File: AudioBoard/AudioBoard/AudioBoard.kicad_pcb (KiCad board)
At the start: 2 copper layers, 14 parts, among them U5 TL072

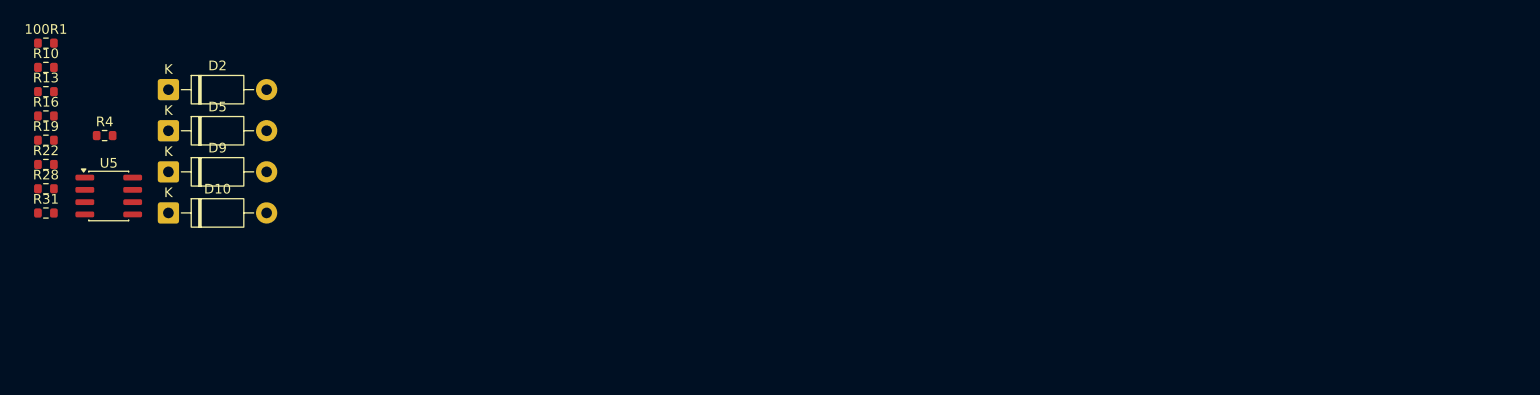
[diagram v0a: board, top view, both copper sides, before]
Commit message: input section with templates are working
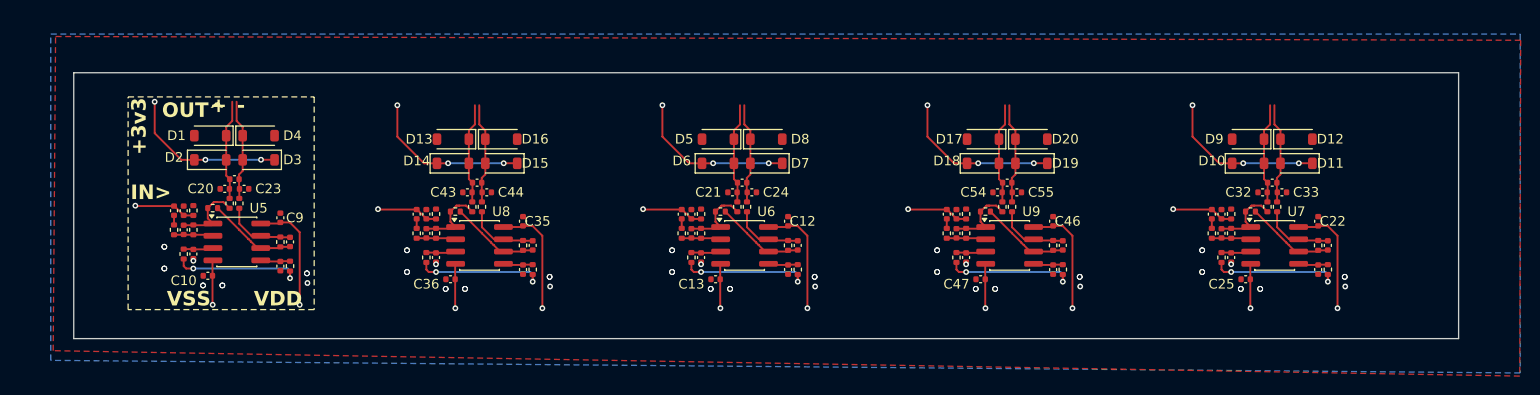
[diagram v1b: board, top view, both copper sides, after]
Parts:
- added 100R2: 1k, Resistor_SMD:R_0402_1005Metric, F.Cu at (112.5, 63.1)
- added 100R3: 1k, Resistor_SMD:R_0402_1005Metric, F.Cu at (167.3, 63.1)
- added 100R4: 1k, Resistor_SMD:R_0402_1005Metric, F.Cu at (85.1, 63.1)
- added 100R5: 1k, Resistor_SMD:R_0402_1005Metric, F.Cu at (139.9, 63.1)
- added C10: 100n, Capacitor_SMD:C_0402_1005Metric, F.Cu at (51.5, 63.8)
- added C11: 1p, Capacitor_SMD:C_0402_1005Metric, F.Cu at (49.0, 59.0)
- added C12: 100n, Capacitor_SMD:C_0402_1005Metric, F.Cu at (111.5, 58.1)
- added C13: 100n, Capacitor_SMD:C_0402_1005Metric, F.Cu at (104.0, 64.1)
- added C14: 100p, Capacitor_SMD:C_0402_1005Metric, F.Cu at (60.0, 60.2)
- added C15: 100n, Capacitor_SMD:C_0402_1005Metric, F.Cu at (102.5, 61.9)
- added C16: 1p, Capacitor_SMD:C_0402_1005Metric, F.Cu at (101.5, 59.4)
- added C17: 100n, Capacitor_SMD:C_0402_1005Metric, F.Cu at (59.0, 62.8)
- added C18: 100n, Capacitor_SMD:C_0402_1005Metric, F.Cu at (111.5, 63.1)
- added C19: 100p, Capacitor_SMD:C_0402_1005Metric, F.Cu at (112.5, 60.6)
- added C2: 100p, Capacitor_SMD:C_0402_1005Metric, F.Cu at (49.0, 57.0)
- added C20: 1n, Capacitor_SMD:C_0402_1005Metric, F.Cu at (53.2, 54.8)
- added C21: 1n, Capacitor_SMD:C_0402_1005Metric, F.Cu at (105.8, 55.1)
- added C22: 100n, Capacitor_SMD:C_0402_1005Metric, F.Cu at (166.3, 58.1)
- added C23: 1n, Capacitor_SMD:C_0402_1005Metric, F.Cu at (55.2, 54.8)
- added C24: 1n, Capacitor_SMD:C_0402_1005Metric, F.Cu at (107.8, 55.1)
- added C25: 100n, Capacitor_SMD:C_0402_1005Metric, F.Cu at (158.8, 64.1)
- added C26: 100p, Capacitor_SMD:C_0402_1005Metric, F.Cu at (54.2, 53.8)
- added C27: 100p, Capacitor_SMD:C_0402_1005Metric, F.Cu at (106.8, 54.1)
- added C28: 100n, Capacitor_SMD:C_0402_1005Metric, F.Cu at (157.3, 61.9)
- added C29: 1p, Capacitor_SMD:C_0402_1005Metric, F.Cu at (156.3, 59.4)
- added C3: 100p, Capacitor_SMD:C_0402_1005Metric, F.Cu at (101.5, 57.4)
- added C30: 100n, Capacitor_SMD:C_0402_1005Metric, F.Cu at (166.3, 63.1)
- added C31: 100p, Capacitor_SMD:C_0402_1005Metric, F.Cu at (167.3, 60.6)
- added C32: 1n, Capacitor_SMD:C_0402_1005Metric, F.Cu at (160.6, 55.1)
- added C33: 1n, Capacitor_SMD:C_0402_1005Metric, F.Cu at (162.6, 55.1)
- added C34: 100p, Capacitor_SMD:C_0402_1005Metric, F.Cu at (161.6, 54.1)
- added C35: 100n, Capacitor_SMD:C_0402_1005Metric, F.Cu at (84.1, 58.1)
- added C36: 100n, Capacitor_SMD:C_0402_1005Metric, F.Cu at (76.6, 64.1)
- added C37: 100p, Capacitor_SMD:C_0402_1005Metric, F.Cu at (74.1, 57.4)
- added C38: 100n, Capacitor_SMD:C_0402_1005Metric, F.Cu at (73.1, 57.4)
- added C39: 100n, Capacitor_SMD:C_0402_1005Metric, F.Cu at (75.1, 61.9)
- added C4: 100p, Capacitor_SMD:C_0402_1005Metric, F.Cu at (156.3, 57.4)
- added C40: 1p, Capacitor_SMD:C_0402_1005Metric, F.Cu at (74.1, 59.4)
- added C41: 100n, Capacitor_SMD:C_0402_1005Metric, F.Cu at (84.1, 63.1)
- added C42: 100p, Capacitor_SMD:C_0402_1005Metric, F.Cu at (85.1, 60.6)
- added C43: 1n, Capacitor_SMD:C_0402_1005Metric, F.Cu at (78.3, 55.1)
- added C44: 1n, Capacitor_SMD:C_0402_1005Metric, F.Cu at (80.3, 55.1)
- added C45: 100p, Capacitor_SMD:C_0402_1005Metric, F.Cu at (79.3, 54.1)
- added C46: 100n, Capacitor_SMD:C_0402_1005Metric, F.Cu at (138.9, 58.1)
- added C47: 100n, Capacitor_SMD:C_0402_1005Metric, F.Cu at (131.4, 64.1)
- added C48: 100p, Capacitor_SMD:C_0402_1005Metric, F.Cu at (128.9, 57.4)
- added C49: 100n, Capacitor_SMD:C_0402_1005Metric, F.Cu at (127.9, 57.4)
- added C5: 100n, Capacitor_SMD:C_0402_1005Metric, F.Cu at (48.0, 57.0)
- added C50: 100n, Capacitor_SMD:C_0402_1005Metric, F.Cu at (129.9, 61.9)
- added C51: 1p, Capacitor_SMD:C_0402_1005Metric, F.Cu at (128.9, 59.4)
- added C52: 100n, Capacitor_SMD:C_0402_1005Metric, F.Cu at (138.9, 63.1)
- added C53: 100p, Capacitor_SMD:C_0402_1005Metric, F.Cu at (139.9, 60.6)
- added C54: 1n, Capacitor_SMD:C_0402_1005Metric, F.Cu at (133.2, 55.1)
- added C55: 1n, Capacitor_SMD:C_0402_1005Metric, F.Cu at (135.2, 55.1)
- added C56: 100p, Capacitor_SMD:C_0402_1005Metric, F.Cu at (134.2, 54.1)
- added C6: 100n, Capacitor_SMD:C_0402_1005Metric, F.Cu at (100.5, 57.4)
- added C7: 100n, Capacitor_SMD:C_0402_1005Metric, F.Cu at (155.3, 57.4)
- added C8: 100n, Capacitor_SMD:C_0402_1005Metric, F.Cu at (50.0, 61.5)
- added C9: 100n, Capacitor_SMD:C_0402_1005Metric, F.Cu at (59.0, 57.8)
- added D1: 1N4148W, Diode_SMD:D_SOD-123, F.Cu at (51.8, 51.8)
- added D11: 1N4148W, Diode_SMD:D_SOD-123, F.Cu at (164.1, 52.1)
- added D12: 1N4148W, Diode_SMD:D_SOD-123, F.Cu at (164.1, 49.6)
- added D13: 1N4148W, Diode_SMD:D_SOD-123, F.Cu at (76.8, 52.1)
- added D14: 1N4148W, Diode_SMD:D_SOD-123, F.Cu at (76.8, 49.6)
- added D15: 1N4148W, Diode_SMD:D_SOD-123, F.Cu at (81.8, 52.1)
- added D16: 1N4148W, Diode_SMD:D_SOD-123, F.Cu at (81.8, 49.6)
- added D17: 1N4148W, Diode_SMD:D_SOD-123, F.Cu at (131.7, 52.1)
- added D18: 1N4148W, Diode_SMD:D_SOD-123, F.Cu at (131.7, 49.6)
- added D19: 1N4148W, Diode_SMD:D_SOD-123, F.Cu at (136.7, 52.1)
- added D20: 1N4148W, Diode_SMD:D_SOD-123, F.Cu at (136.7, 49.6)
- added D3: 1N4148W, Diode_SMD:D_SOD-123, F.Cu at (56.8, 51.8)
- added D4: 1N4148W, Diode_SMD:D_SOD-123, F.Cu at (56.8, 49.3)
- added D6: 1N4148W, Diode_SMD:D_SOD-123, F.Cu at (104.3, 49.6)
- added D7: 1N4148W, Diode_SMD:D_SOD-123, F.Cu at (109.3, 52.1)
- added D8: 1N4148W, Diode_SMD:D_SOD-123, F.Cu at (109.3, 49.6)
- added R11: 1M, Resistor_SMD:R_0402_1005Metric, F.Cu at (100.5, 59.4)
- added R12: 1M, Resistor_SMD:R_0402_1005Metric, F.Cu at (155.3, 59.4)
- added R14: 100R, Resistor_SMD:R_0402_1005Metric, F.Cu at (101.5, 61.9)
- added R15: 100R, Resistor_SMD:R_0402_1005Metric, F.Cu at (156.3, 61.9)
- added R17: 510k, Resistor_SMD:R_0402_1005Metric, F.Cu at (102.5, 59.4)
- added R18: 510k, Resistor_SMD:R_0402_1005Metric, F.Cu at (157.3, 59.4)
- added R20: 4k7, Resistor_SMD:R_0402_1005Metric, F.Cu at (104.5, 57.1)
- added R21: 4k7, Resistor_SMD:R_0402_1005Metric, F.Cu at (159.3, 57.1)
- added R23: 4k7, Resistor_SMD:R_0402_1005Metric, F.Cu at (111.5, 60.6)
- added R24: 4k7, Resistor_SMD:R_0402_1005Metric, F.Cu at (166.3, 60.6)
- added R25: 1M, Resistor_SMD:R_0402_1005Metric, F.Cu at (73.1, 59.4)
- added R26: 100R, Resistor_SMD:R_0402_1005Metric, F.Cu at (74.1, 61.9)
- added R27: 510k, Resistor_SMD:R_0402_1005Metric, F.Cu at (75.1, 59.4)
- added R29: 100R, Resistor_SMD:R_0402_1005Metric, F.Cu at (107.3, 56.6)
- added R30: 100R, Resistor_SMD:R_0402_1005Metric, F.Cu at (162.1, 56.6)
- added R32: 100R, Resistor_SMD:R_0402_1005Metric, F.Cu at (106.3, 56.6)
- added R33: 100R, Resistor_SMD:R_0402_1005Metric, F.Cu at (161.1, 56.6)
- added R34: 4k7, Resistor_SMD:R_0402_1005Metric, F.Cu at (77.1, 57.1)
- added R35: 4k7, Resistor_SMD:R_0402_1005Metric, F.Cu at (84.1, 60.6)
- added R36: 100R, Resistor_SMD:R_0402_1005Metric, F.Cu at (79.8, 56.6)
- added R37: 100R, Resistor_SMD:R_0402_1005Metric, F.Cu at (78.8, 56.6)
- added R38: 1M, Resistor_SMD:R_0402_1005Metric, F.Cu at (127.9, 59.4)
- added R39: 100R, Resistor_SMD:R_0402_1005Metric, F.Cu at (128.9, 61.9)
- added R40: 510k, Resistor_SMD:R_0402_1005Metric, F.Cu at (129.9, 59.4)
- added R41: 4k7, Resistor_SMD:R_0402_1005Metric, F.Cu at (131.9, 57.1)
- added R42: 4k7, Resistor_SMD:R_0402_1005Metric, F.Cu at (138.9, 60.6)
- added R43: 100R, Resistor_SMD:R_0402_1005Metric, F.Cu at (134.7, 56.6)
- added R44: 100R, Resistor_SMD:R_0402_1005Metric, F.Cu at (133.7, 56.6)
- added R5: 100R, Resistor_SMD:R_0402_1005Metric, F.Cu at (102.5, 57.4)
- added R6: 100R, Resistor_SMD:R_0402_1005Metric, F.Cu at (157.3, 57.4)
- added R7: 100R, Resistor_SMD:R_0402_1005Metric, F.Cu at (75.1, 57.4)
- added R8: 100R, Resistor_SMD:R_0402_1005Metric, F.Cu at (129.9, 57.4)
- added U6: TL072, Package_SO:SOIC-8_3.9x4.9mm_P1.27mm, F.Cu at (107.0, 60.6)
- added U7: TL072, Package_SO:SOIC-8_3.9x4.9mm_P1.27mm, F.Cu at (161.8, 60.6)
- added U8: TL072, Package_SO:SOIC-8_3.9x4.9mm_P1.27mm, F.Cu at (79.6, 60.6)
- added U9: TL072, Package_SO:SOIC-8_3.9x4.9mm_P1.27mm, F.Cu at (134.4, 60.6)
- 100R1, R10, R13, R16, R19, R22, R28, R31, R4: footprint Resistor_SMD:R_0603_1608Metric -> Resistor_SMD:R_0402_1005Metric
- D10, D2, D5, D9: value 1N5819 -> 1N4148W; footprint Diode_THT:D_DO-41_SOD81_P10.16mm_Horizontal -> Diode_SMD:D_SOD-123
- moved D10 111.9 mm to (159.1, 49.6), turned to 180 degrees
- moved D9 111.7 mm to (159.1, 52.1)
- moved D5 56.9 mm to (104.3, 52.1)
- moved 100R1 34.2 mm to (60.0, 62.8), turned to -90 degrees
- moved R22 25.5 mm to (59.0, 60.2), turned to 90 degrees
- moved R13 22.0 mm to (49.0, 61.5), turned to 90 degrees
- moved R10 21.4 mm to (48.0, 59.0), turned to -90 degrees
- moved R28 20.1 mm to (54.8, 56.3), turned to 90 degrees
- moved R16 19.3 mm to (50.0, 59.0), turned to 90 degrees
- moved R31 19.0 mm to (53.8, 56.3), turned to 90 degrees
- moved R19 18.6 mm to (52.0, 56.8)
- moved U5 14.1 mm to (54.5, 60.2)
- moved R4 12.0 mm to (50.0, 57.0), turned to -90 degrees
- moved D2 6.43 mm to (51.8, 49.3), turned to 180 degrees
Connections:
- D10 pad 1: /Instrument_Input1/OUT_N -> /Instrument_Input3/OUT_P
- D2 pad 1: /Instrument_Input1/+3V3 -> /Instrument_Input1/OUT_P
- D2 pad 2: /Instrument_Input1/OUT_P -> GND
- D5 pad 1: /Instrument_Input1/OUT_P -> /Instrument_Input2/+3V3
- D5 pad 2: GND -> /Instrument_Input2/OUT_P
- D9 pad 1: /Instrument_Input1/+3V3 -> /Instrument_Input3/+3V3
- D9 pad 2: /Instrument_Input1/OUT_N -> /Instrument_Input3/OUT_P
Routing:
- net /Instrument_Input5/+3V3: track 0.00 -> 16.8 mm, vias 0 -> 3
- net /Instrument_Input4/+3V3: track 0.00 -> 16.8 mm, vias 0 -> 3
- net /Instrument_Input3/+3V3: track 0.00 -> 16.8 mm, vias 0 -> 3
- net /Instrument_Input2/+3V3: track 0.00 -> 16.8 mm, vias 0 -> 3
- net /Instrument_Input1/+3V3: track 0.00 -> 16.8 mm, vias 0 -> 3
- net /Instrument_Input5/BIAS: track 0.00 -> 13.4 mm, vias 0 -> 2
- net /Instrument_Input4/BIAS: track 0.00 -> 13.4 mm, vias 0 -> 2
- net /Instrument_Input3/BIAS: track 0.00 -> 13.4 mm, vias 0 -> 2
- net /Instrument_Input2/BIAS: track 0.00 -> 13.4 mm, vias 0 -> 2
- net /Instrument_Input1/BIAS: track 0.00 -> 13.4 mm, vias 0 -> 2
- net /Instrument_Input3/VDD: track 0.00 -> 12.0 mm, vias 0 -> 1
- net /Instrument_Input1/VDD: track 0.00 -> 12.0 mm, vias 0 -> 1
- net /Instrument_Input5/VDD: track 0.00 -> 12.0 mm, vias 0 -> 1
- net /Instrument_Input4/VDD: track 0.00 -> 12.0 mm, vias 0 -> 1
- net /Instrument_Input2/VDD: track 0.00 -> 12.0 mm, vias 0 -> 1
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- added copper zone on B.Cu, net GND
- added copper zone on F.Cu, net GND
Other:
- board outline added: 143.2 x 27.5 mm
- copper layers 2 -> 4
- board text added: "+"
- board text added: "+3v3"
- board text added: "-"
- board text added: "IN>"
- board text added: "OUT^"
- board text added: "VDD"
- board text added: "VSS"

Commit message: Created input sections
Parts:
- moved 100R1 77.7 mm to (122.2, 109.4)
- moved 100R3 77.7 mm to (229.5, 109.8)
- moved 100R4 77.7 mm to (147.2, 109.8)
- moved 100R5 77.7 mm to (202.1, 109.8)
- moved C10 77.7 mm to (113.7, 110.4)
- moved C11 77.7 mm to (111.2, 105.7)
- moved C14 77.7 mm to (122.2, 106.9)
- moved C17 77.7 mm to (121.2, 109.4)
- moved C2 77.7 mm to (111.2, 103.7)
- moved C20 77.7 mm to (115.4, 101.4)
- moved C22 77.7 mm to (228.5, 104.8)
- moved C23 77.7 mm to (117.4, 101.4)
- moved C25 77.7 mm to (221.0, 110.8)
- moved C26 77.7 mm to (116.4, 100.4)
- moved C28 77.7 mm to (219.5, 108.5)
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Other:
- board size 143.2 x 27.5 mm -> 240 x 100 mm

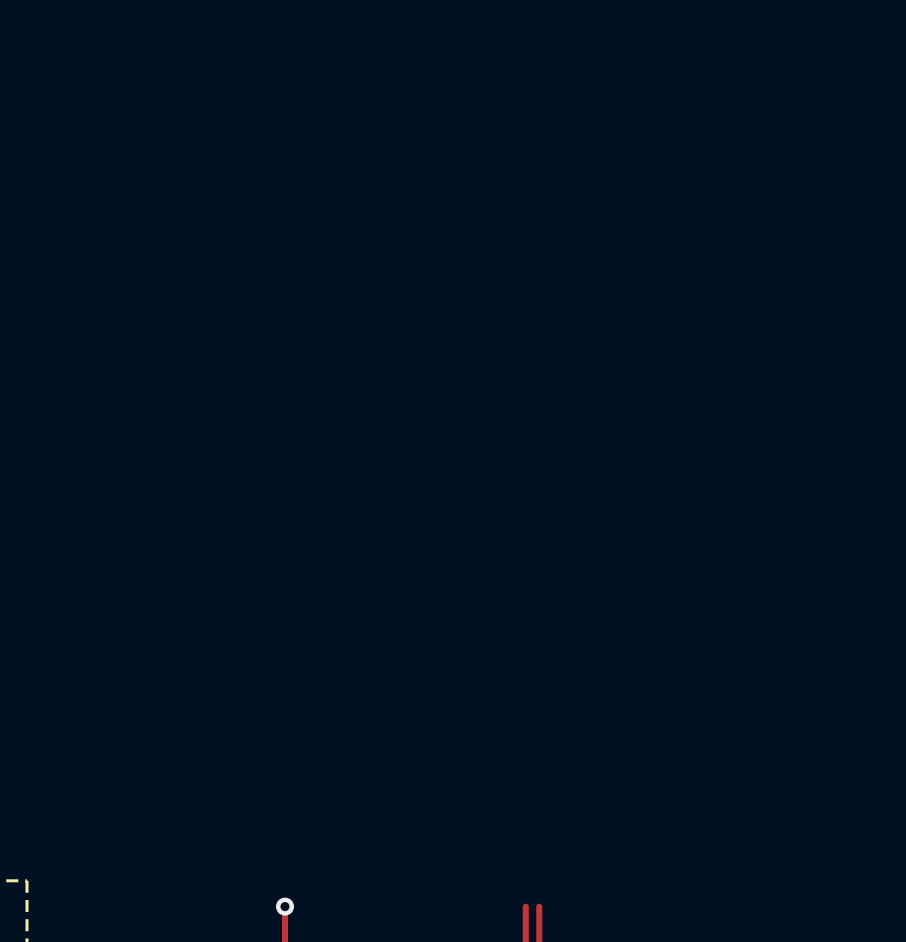
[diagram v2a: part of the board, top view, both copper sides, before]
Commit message: xlr frontends added
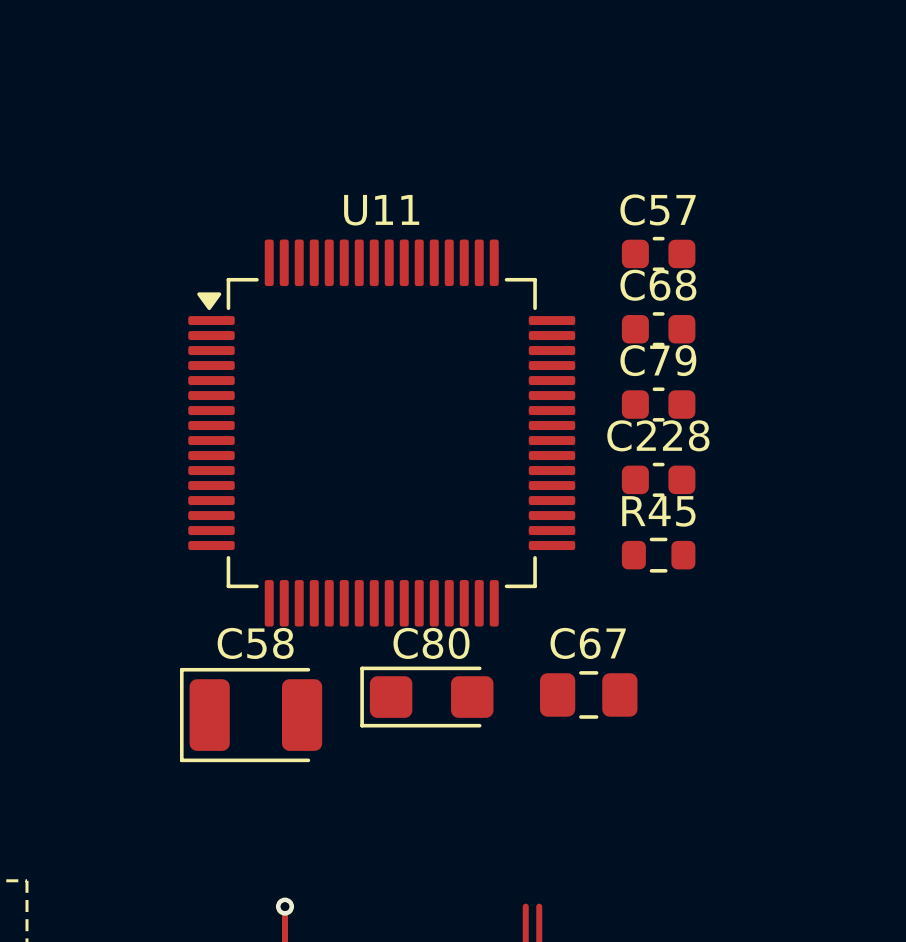
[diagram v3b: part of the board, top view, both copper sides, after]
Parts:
- added C228: 1nF, Capacitor_SMD:C_0603_1608Metric, F.Cu at (145.7, 78.5)
- added C57: 100nF, Capacitor_SMD:C_0603_1608Metric, F.Cu at (145.7, 71.0)
- added C58: 100uF tantal, Capacitor_Tantalum_SMD:CP_EIA-3528-21_Kemet-B, F.Cu at (132.3, 86.4)
- added C67: 33nF, Capacitor_SMD:C_0805_2012Metric_Pad1.18x1.45mm_HandSolder, F.Cu at (143.4, 85.7)
- added C68: 1nF, Capacitor_SMD:C_0603_1608Metric, F.Cu at (145.7, 73.5)
- added C79: 100nF, Capacitor_SMD:C_0603_1608Metric, F.Cu at (145.7, 76.0)
- added C80: 10uF tantal, Capacitor_Tantalum_SMD:CP_EIA-3216-18_Kemet-A, F.Cu at (138.1, 85.8)
- added R45: 3k, Resistor_SMD:R_0603_1608Metric, F.Cu at (145.7, 81.0)
- added U11: ~, Package_QFP:LQFP-64_10x10mm_P0.5mm, F.Cu at (136.5, 77.0)
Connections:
- R5 pad 1: /Instrument_Input1/IN -> /Instrument_Input2/IN

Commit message: added dxf file to pcb view
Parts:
- removed U11: ~, Package_QFP:LQFP-64_10x10mm_P0.5mm
- added 100R6: 1k, Resistor_SMD:R_0402_1005Metric, F.Cu at (208.7, 183.6)
- added C108: 470pF, Capacitor_SMD:C_0603_1608Metric, F.Cu at (207.7, 149.8)
- added C109: 470pF, Capacitor_SMD:C_0603_1608Metric, F.Cu at (207.7, 152.3)
- added C110: 100pF, Capacitor_SMD:C_0603_1608Metric, F.Cu at (207.7, 154.8)
- added C111: 100pF, Capacitor_SMD:C_0603_1608Metric, F.Cu at (207.7, 157.3)
- added C112: 2.2uF, Capacitor_SMD:C_0805_2012Metric_Pad1.18x1.45mm_HandSolder, F.Cu at (216.1, 150.0)
- added C113: 470pF, Capacitor_SMD:C_0603_1608Metric, F.Cu at (207.7, 166.8)
- added C114: 470pF, Capacitor_SMD:C_0603_1608Metric, F.Cu at (207.7, 169.3)
- added C115: 100pF, Capacitor_SMD:C_0603_1608Metric, F.Cu at (207.7, 171.8)
- added C116: 100pF, Capacitor_SMD:C_0603_1608Metric, F.Cu at (207.7, 174.3)
- added C117: 2.2uF, Capacitor_SMD:C_0805_2012Metric_Pad1.18x1.45mm_HandSolder, F.Cu at (216.1, 167.1)
- added C118: 470pF, Capacitor_SMD:C_0603_1608Metric, F.Cu at (178.0, 149.8)
- added C119: 470pF, Capacitor_SMD:C_0603_1608Metric, F.Cu at (178.0, 152.3)
- added C120: 100pF, Capacitor_SMD:C_0603_1608Metric, F.Cu at (178.0, 154.8)
- added C121: 100pF, Capacitor_SMD:C_0603_1608Metric, F.Cu at (178.0, 157.3)
- added C122: 2.2uF, Capacitor_SMD:C_0805_2012Metric_Pad1.18x1.45mm_HandSolder, F.Cu at (186.4, 150.0)
- added C123: 470pF, Capacitor_SMD:C_0603_1608Metric, F.Cu at (192.8, 149.8)
- added C124: 470pF, Capacitor_SMD:C_0603_1608Metric, F.Cu at (192.8, 152.3)
- added C125: 100pF, Capacitor_SMD:C_0603_1608Metric, F.Cu at (192.8, 154.8)
- added C126: 100pF, Capacitor_SMD:C_0603_1608Metric, F.Cu at (192.8, 157.3)
- added C127: 2.2uF, Capacitor_SMD:C_0805_2012Metric_Pad1.18x1.45mm_HandSolder, F.Cu at (201.3, 150.0)
- added C140: 470pF, Capacitor_SMD:C_0603_1608Metric, F.Cu at (192.8, 166.8)
- added C141: 470pF, Capacitor_SMD:C_0603_1608Metric, F.Cu at (192.8, 169.3)
- added C142: 470pF, Capacitor_SMD:C_0603_1608Metric, F.Cu at (178.0, 166.8)
- added C143: 470pF, Capacitor_SMD:C_0603_1608Metric, F.Cu at (178.0, 169.3)
- added C144: 100pF, Capacitor_SMD:C_0603_1608Metric, F.Cu at (192.8, 171.8)
- added C145: 100pF, Capacitor_SMD:C_0603_1608Metric, F.Cu at (192.8, 174.3)
- added C146: 100pF, Capacitor_SMD:C_0603_1608Metric, F.Cu at (178.0, 171.8)
- added C147: 2.2uF, Capacitor_SMD:C_0805_2012Metric_Pad1.18x1.45mm_HandSolder, F.Cu at (201.3, 167.1)
- added C148: 100pF, Capacitor_SMD:C_0603_1608Metric, F.Cu at (178.0, 174.3)
- added C149: 2.2uF, Capacitor_SMD:C_0805_2012Metric_Pad1.18x1.45mm_HandSolder, F.Cu at (186.4, 167.1)
- added C59: 100n, Capacitor_SMD:C_0402_1005Metric, F.Cu at (185.5, 169.6)
- added C61: 100n, Capacitor_SMD:C_0402_1005Metric, F.Cu at (200.3, 169.6)
- added C62: 100n, Capacitor_SMD:C_0402_1005Metric, F.Cu at (185.5, 171.5)
- added R103: 3k, Resistor_SMD:R_0603_1608Metric, F.Cu at (192.8, 176.9)
- added R104: 3k, Resistor_SMD:R_0603_1608Metric, F.Cu at (192.8, 179.4)
- added R105: 3k, Resistor_SMD:R_0603_1608Metric, F.Cu at (178.0, 176.9)
- added R106: 3k, Resistor_SMD:R_0603_1608Metric, F.Cu at (178.0, 179.4)
- added R107: 3k, Resistor_SMD:R_0603_1608Metric, F.Cu at (196.8, 166.8)
- added R108: 3k, Resistor_SMD:R_0603_1608Metric, F.Cu at (196.8, 169.3)
- added R109: 3k, Resistor_SMD:R_0603_1608Metric, F.Cu at (182.0, 166.8)
- added R110: 3k, Resistor_SMD:R_0603_1608Metric, F.Cu at (182.0, 169.3)
- added R111: 3k, Resistor_SMD:R_0603_1608Metric, F.Cu at (196.8, 171.8)
- added R112: 3k, Resistor_SMD:R_0603_1608Metric, F.Cu at (196.8, 174.3)
- added R113: 3k, Resistor_SMD:R_0603_1608Metric, F.Cu at (182.0, 171.8)
- added R114: 1k, Resistor_SMD:R_0603_1608Metric, F.Cu at (196.8, 176.9)
- added R115: 3k, Resistor_SMD:R_0603_1608Metric, F.Cu at (182.0, 174.3)
- added R116: 1k, Resistor_SMD:R_0603_1608Metric, F.Cu at (182.0, 176.9)
- added R59: 3k, Resistor_SMD:R_0603_1608Metric, F.Cu at (207.7, 159.8)
- added R60: 3k, Resistor_SMD:R_0603_1608Metric, F.Cu at (207.7, 162.3)
- added R61: 3k, Resistor_SMD:R_0603_1608Metric, F.Cu at (211.7, 149.8)
- added R62: 3k, Resistor_SMD:R_0603_1608Metric, F.Cu at (211.7, 152.3)
- added R63: 3k, Resistor_SMD:R_0603_1608Metric, F.Cu at (211.7, 154.8)
- added R64: 3k, Resistor_SMD:R_0603_1608Metric, F.Cu at (211.7, 157.3)
- added R65: 1k, Resistor_SMD:R_0603_1608Metric, F.Cu at (211.7, 159.8)
- added R66: 3k, Resistor_SMD:R_0603_1608Metric, F.Cu at (207.7, 176.9)
- added R67: 3k, Resistor_SMD:R_0603_1608Metric, F.Cu at (207.7, 179.4)
- added R68: 3k, Resistor_SMD:R_0603_1608Metric, F.Cu at (211.7, 166.8)
- added R69: 3k, Resistor_SMD:R_0603_1608Metric, F.Cu at (211.7, 169.3)
- added R70: 3k, Resistor_SMD:R_0603_1608Metric, F.Cu at (211.7, 171.8)
- added R71: 3k, Resistor_SMD:R_0603_1608Metric, F.Cu at (211.7, 174.3)
- added R72: 1k, Resistor_SMD:R_0603_1608Metric, F.Cu at (211.7, 176.9)
- added R73: 3k, Resistor_SMD:R_0603_1608Metric, F.Cu at (178.0, 159.8)
- added R74: 3k, Resistor_SMD:R_0603_1608Metric, F.Cu at (178.0, 162.3)
- added R75: 3k, Resistor_SMD:R_0603_1608Metric, F.Cu at (182.0, 149.8)
- added R76: 3k, Resistor_SMD:R_0603_1608Metric, F.Cu at (182.0, 152.3)
- added R77: 3k, Resistor_SMD:R_0603_1608Metric, F.Cu at (182.0, 154.8)
- added R78: 3k, Resistor_SMD:R_0603_1608Metric, F.Cu at (182.0, 157.3)
- added R79: 1k, Resistor_SMD:R_0603_1608Metric, F.Cu at (182.0, 159.8)
- added R80: 3k, Resistor_SMD:R_0603_1608Metric, F.Cu at (192.8, 159.8)
- added R81: 3k, Resistor_SMD:R_0603_1608Metric, F.Cu at (192.8, 162.3)
- added R82: 3k, Resistor_SMD:R_0603_1608Metric, F.Cu at (196.8, 149.8)
- added R83: 3k, Resistor_SMD:R_0603_1608Metric, F.Cu at (196.8, 152.3)
- added R84: 3k, Resistor_SMD:R_0603_1608Metric, F.Cu at (196.8, 154.8)
- added R85: 3k, Resistor_SMD:R_0603_1608Metric, F.Cu at (196.8, 157.3)
- added R86: 1k, Resistor_SMD:R_0603_1608Metric, F.Cu at (196.8, 159.8)
- added R9: 820R, Resistor_SMD:R_0402_1005Metric, F.Cu at (208.7, 185.6)
- added U1: ~, Package_QFP:LQFP-64_10x10mm_P0.5mm, F.Cu at (198.1, 189.8)
- C37, C42, C48, C53, C56: value 100p -> 100n
- C40: value 1p -> 47u
- C46: value 100n -> 47u
- C47, C50: value 100n -> 100p
- C51: value 1p -> 100p
- C54: value 1n -> 100n
- R38: value 1M -> 47
- R39: value 100R -> 2k2
- R40: value 510k -> 2k2
- R41, R42: value 4k7 -> 2k2
- R8: value 100R -> 820R
- moved C228 120.4 mm to (180.5, 193.8)
- moved C57 120.4 mm to (180.5, 186.3)
- moved C79 120.4 mm to (180.5, 191.3)
- moved C68 120.4 mm to (180.5, 188.8)
- moved R45 120.4 mm to (180.5, 196.3)
- moved C67 116.0 mm to (184.9, 194.0)
- moved C80 115.3 mm to (185.4, 190.9)
- moved C58 114.0 mm to (185.5, 187.2)
- moved C49 102.1 mm to (285.5, 140.2), turned to 90 degrees
- moved D18 102.0 mm to (281.8, 148.0), turned to 0 degrees
- moved R38 100.7 mm to (285.5, 138.2), turned to 90 degrees
- moved C48 100.2 mm to (284.5, 140.2), turned to -90 degrees
- moved D17 99.6 mm to (281.8, 145.5), turned to 180 degrees
- moved C51 98.8 mm to (284.5, 138.2), turned to -90 degrees
- moved R8 98.3 mm to (283.5, 140.2), turned to 90 degrees
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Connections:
- net /Instrument_Input1/IN renamed /Instrument_Input/IN
- net /Instrument_Input1/OUT_N renamed /Instrument_Input/OUT_N
- net /Instrument_Input1/OUT_P renamed /Instrument_Input/OUT_P
- net /Instrument_Input2/IN renamed /Instrument_L1_return/IN
- net /Instrument_Input2/OUT_N renamed /Instrument_L1_return/OUT_N
- net /Instrument_Input2/OUT_P renamed /Instrument_L1_return/OUT_P
- net /Instrument_Input3/IN renamed /Instrument_L2_return/IN
- net /Instrument_Input3/OUT_N renamed /Instrument_L2_return/OUT_N
- net /Instrument_Input3/OUT_P renamed /Instrument_L2_return/OUT_P
- net /Instrument_Input4/OUT_N renamed /MIC_preamp/OUT_N
- net /Instrument_Input4/OUT_P renamed /MIC_preamp/OUT_P
- 100R1 pad 2: /Instrument_Input1/BIAS -> VBIAS
- 100R2 pad 2: /Instrument_Input2/BIAS -> VBIAS
- 100R3 pad 2: /Instrument_Input3/BIAS -> VBIAS
- 100R5 pad 1: Net-(U9B-+) -> Net-(U2B-+)
- 100R5 pad 2: /Instrument_Input5/BIAS -> VBIAS
- C10 pad 1: /Instrument_Input1/VSS -> VSS
- C12 pad 1: /Instrument_Input2/VDD -> VDD
- C13 pad 1: /Instrument_Input2/VSS -> VSS
- C22 pad 1: /Instrument_Input3/VDD -> VDD
- C228 pad 1: +3.3VA -> AVDD
- C25 pad 1: /Instrument_Input3/VSS -> VSS
- C35 pad 1: /Instrument_Input4/VDD -> VDD
- C36 pad 1: /Instrument_Input4/VSS -> VSS
- C37 pad 1: Net-(C37-Pad1) -> VDD
- C38 pad 1: Net-(C37-Pad1) -> VSS
- C38 pad 2: Net-(C38-Pad2) -> GND
- C39 pad 1: Net-(U8A-+) -> VDD
- C40 pad 1: Net-(U8A--) -> /MIC_preamp/IN_P
- C40 pad 2: Net-(C40-Pad2) -> Net-(U2B--)
- C41 pad 1: Net-(U8B-+) -> VSS
- C42 pad 1: Net-(U8B--) -> VDD
- C42 pad 2: Net-(C42-Pad2) -> GND
- C46 pad 1: /Instrument_Input5/VDD -> /MIC_preamp/IN_N
- C46 pad 2: GND -> Net-(U3A--)
- C47 pad 1: /Instrument_Input5/VSS -> Net-(U3A--)
- C47 pad 2: GND -> Net-(U2B--)
- C48 pad 1: Net-(C48-Pad1) -> Net-(U2B-+)
- C49 pad 1: Net-(C48-Pad1) -> Net-(U3A-+)
- C49 pad 2: Net-(C49-Pad2) -> GND
- C50 pad 1: Net-(U9A-+) -> Net-(U2B--)
- C50 pad 2: GND -> Net-(C50-Pad2)
- C51 pad 1: Net-(U9A--) -> Net-(U3A--)
- C52 pad 1: Net-(U9B-+) -> VSS
- C53 pad 1: Net-(U9B--) -> VDD
- C53 pad 2: Net-(C53-Pad2) -> GND
- C54 pad 1: GND -> VSS
- C54 pad 2: /Instrument_Input5/OUT_P -> GND
- C56 pad 1: /Instrument_Input5/OUT_N -> VDD
- C56 pad 2: /Instrument_Input5/OUT_P -> GND
- C57 pad 2: AD1939_CM -> VBIAS
- C58 pad 1: AD1939_CM -> VBIAS
- C68 pad 1: +3.3VA -> AVDD
- C9 pad 1: /Instrument_Input1/VDD -> VDD
- D1 pad 1: /Instrument_Input1/+3V3 -> AVDD
- D11 pad 1: /Instrument_Input3/+3V3 -> AVDD
- D13 pad 1: /Instrument_Input4/+3V3 -> AVDD
- D15 pad 1: /Instrument_Input4/+3V3 -> AVDD
- D3 pad 1: /Instrument_Input1/+3V3 -> AVDD
- D5 pad 1: /Instrument_Input2/+3V3 -> AVDD
- D7 pad 1: /Instrument_Input2/+3V3 -> AVDD
- D9 pad 1: /Instrument_Input3/+3V3 -> AVDD
- R13 pad 1: /Instrument_Input1/BIAS -> VBIAS
- R14 pad 1: /Instrument_Input2/BIAS -> VBIAS
- R15 pad 1: /Instrument_Input3/BIAS -> VBIAS
- R36 pad 1: Net-(C42-Pad2) -> Net-(C51-Pad2)
- R37 pad 1: Net-(C40-Pad2) -> Net-(C50-Pad2)
- R38 pad 1: Net-(C49-Pad2) -> Net-(SW1-B)
- R38 pad 2: Net-(U9A--) -> Net-(C1-Pad1)
- R39 pad 1: /Instrument_Input5/BIAS -> GND
- R39 pad 2: Net-(U9A-+) -> Net-(U2B--)
- R40 pad 1: Net-(U9A--) -> Net-(U3A--)
- R40 pad 2: Net-(C51-Pad2) -> GND
- R41 pad 1: Net-(C51-Pad2) -> Net-(C50-Pad2)
- R41 pad 2: Net-(U9B--) -> Net-(U2B--)
- R42 pad 1: Net-(U9B--) -> Net-(C51-Pad2)
- R42 pad 2: Net-(C53-Pad2) -> Net-(U3A--)
- R45 pad 2: +3.3VA -> AVDD
- R8 pad 1: /Instrument_Input5/IN -> Net-(C1-Pad1)
- R8 pad 2: Net-(C48-Pad1) -> /MIC_preamp/IN_P
- U5 pad 4: /Instrument_Input1/VSS -> VSS
- U5 pad 8: /Instrument_Input1/VDD -> VDD
- U6 pad 4: /Instrument_Input2/VSS -> VSS
- U6 pad 8: /Instrument_Input2/VDD -> VDD
- U7 pad 4: /Instrument_Input3/VSS -> VSS
- U7 pad 8: /Instrument_Input3/VDD -> VDD
- U8 pad 1: Net-(C40-Pad2) -> Net-(C115-Pad2)
- U8 pad 4: /Instrument_Input4/VSS -> VSS
- U8 pad 5: Net-(U8B-+) -> (no net)
- U8 pad 6: Net-(U8B--) -> (no net)
- U8 pad 7: Net-(C42-Pad2) -> (no net)
- U8 pad 8: /Instrument_Input4/VDD -> VDD
- U9 pad 1: Net-(C51-Pad2) -> Net-(C120-Pad2)
- U9 pad 4: /Instrument_Input5/VSS -> VSS
- U9 pad 5: Net-(U9B-+) -> (no net)
- U9 pad 6: Net-(U9B--) -> (no net)
- U9 pad 7: Net-(C53-Pad2) -> (no net)
- U9 pad 8: /Instrument_Input5/VDD -> VDD
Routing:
- net AVDD: track 0.00 -> 67.2 mm, vias 0 -> 12
- net VDD: track 0.00 -> 48.0 mm, vias 0 -> 4
- net VBIAS: track 0.00 -> 40.3 mm, vias 0 -> 6
- net (no net): track 0.00 -> 26.1 mm, vias 0 -> 3
- net VSS: track 0.00 -> 18.5 mm, vias 0 -> 4
- net /Instrument_Input4/+3V3: track 16.8 -> 0.00 mm, vias 3 -> 0
- net /Instrument_Input3/+3V3: track 16.8 -> 0.00 mm, vias 3 -> 0
- net /Instrument_Input2/+3V3: track 16.8 -> 0.00 mm, vias 3 -> 0
- net /Instrument_Input1/+3V3: track 16.8 -> 0.00 mm, vias 3 -> 0
- net GND: track 1.45 -> 15.7 mm, vias 60 -> 61
- net /Instrument_Input5/BIAS: track 13.4 -> 0.00 mm, vias 2 -> 0
- net /Instrument_Input3/BIAS: track 13.4 -> 0.00 mm, vias 2 -> 0
- net /Instrument_Input2/BIAS: track 13.4 -> 0.00 mm, vias 2 -> 0
- net /Instrument_Input1/BIAS: track 13.4 -> 0.00 mm, vias 2 -> 0
- net /Instrument_Input5/VDD: track 12.0 -> 0.00 mm, vias 1 -> 0
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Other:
- board size 240 x 100 mm -> 250 x 160 mm
